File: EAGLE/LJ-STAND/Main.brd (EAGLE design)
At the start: 100 x 80 mm, 74 parts

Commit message: Things
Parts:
- removed MTR2_OUT1, MTR3_OUT2: (no value), jst-vh:B2P-VH
- added MTR2_OUT, MTR3_OUT: (no value), jst-vh:B2P-VH
- added PIXY_I2C, PIXY_SPI: (no value), SparkFun-Connectors:2X5-SHROUDED
- added R3, R4: 4.7K, SparkFun-Resistors:0603-RES
- moved IMU 133.5 mm to (-38.1, 115.6)
- moved R2 132.9 mm to (-54.6, 115.6)
- moved R1 131.8 mm to (-50.8, 115.6)
- moved MOTOR_3 102.9 mm to (-99.1, 14.0)
- moved C28 86.4 mm to (-101.6, 91.4)
- moved TSOP8 79.6 mm to (-96.5, 102.9)
- moved TSOP16 71.7 mm to (-88.9, 111.8)
- moved C17 61.1 mm to (-19.1, 121.9)
- moved C16 61.1 mm to (-15.2, 121.9)
- moved C21 61.1 mm to (-34.3, 121.9)
- moved C22 61.1 mm to (-38.1, 121.9)
- moved C18 61.1 mm to (-22.9, 121.9)
- moved C19 61.1 mm to (-26.7, 121.9)
- moved C20 61.1 mm to (-30.5, 121.9)
- moved C3 31.9 mm to (-66.0, 115.6)
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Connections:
- new net PIXY_CS: MASTER.43, PIXY_SPI.7
- new net PIXY_MISO: MASTER.45, PIXY_SPI.1
- new net PIXY_MOSI: MASTER.44, PIXY_SPI.4
- new net PIXY_SCK: MASTER.46, PIXY_SPI.3
- new net PIXY_SCL: PIXY_I2C.5
- new net PIXY_SDA: PIXY_I2C.9
- new net TEENSY_SCL: MASTER.37, R3.1
- new net TEENSY_SDA: MASTER.38, R4.1
- net +3V3: now also R3.2, R4.2
- net +5V: now also PIXY_I2C.2, PIXY_SPI.2
- net CS_LIGHT_SENSOR: now also LIGHT_SENSOR.10
- net CS_TSOP: now also MASTER.21; no longer MASTER.15
- net GND: now also PIXY_I2C.10, PIXY_I2C.6, PIXY_I2C.8, PIXY_SPI.10, PIXY_SPI.6, PIXY_SPI.8
- net MISO: now also LIGHT_SENSOR.12
- net MOSI: now also LIGHT_SENSOR.11
- net N$1: now also MTR2_OUT.2; no longer MTR2_OUT1.2
- net N$14: now also MTR3_OUT.2; no longer MTR3_OUT2.2
- net N$16: now also MTR3_OUT.1; no longer MTR3_OUT2.1
- net N$2: now also MTR2_OUT.1; no longer MTR2_OUT1.1
- net SCK: now also LIGHT_SENSOR.13
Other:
- board size 100 x 80 mm -> 127.3 x 135.9 mm

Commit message: Stuffs
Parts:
- added Q1, Q2: BSS138, m-pad-2.1:SOT23
- VREG-3.3V: value LM340S-05 -> LM1084
- moved LOGIC_FUSE 121.5 mm to (-123.2, -17.8)
- moved MOTOR_FUSE 105.7 mm to (-123.2, -7.62)
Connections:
- new net TEENSY_SDL: TSOP.37
- net TEENSY_SCL: now also LIGHT_SENSOR.3
- net TEENSY_SDA: now also LIGHT_SENSOR.4, TSOP.38
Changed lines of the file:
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@@
 <?xml version="1.0" encoding="utf-8"?>
 <!DOCTYPE eagle SYSTEM "eagle.dtd">
-<eagle version="7.5.0">
+<eagle version="7.2.0">
 <drawing>
 <settings>
@@
 </element>
 <element name="LIGHT_SENSOR" library="teensy-3.5" package="TEENSY-3.5" value="TEENSY-3.5" x="-22.86" y="31.75"/>
-<element name="LOGIC_FUSE" library="fuse-holder-3568" package="3568-FUSEHOLDER" value="2A" x="-69.85" y="91.44"/>
 <element name="LOGIC_SWITCH" library="jst-vh" package="B2P-VH" value="" x="-74.93" y="69.85"/>
 <element name="MASTER" library="teensy-3.5" package="TEENSY-3.5" value="TEENSY-3.5" x="-41.91" y="31.75"/>
@@
 <element name="MOTOR_2" library="TB6549PG-motor-controller" package="TB6549PG" value="TB6549PG" x="-87.63" y="13.97"/>
 <element name="MOTOR_3" library="TB6549PG-motor-controller" package="TB6549PG" value="TB6549PG" x="-99.06" y="13.97"/>
-<element name="MOTOR_FUSE" library="fuse-holder-3568" package="3568-FUSEHOLDER" value="7.5A" x="-86.36" y="91.44"/>
 <element name="MOTOR_SWITCH" library="jst-vh" package="B2P-VH" value="" x="-59.69" y="69.85"/>
 <element name="MTR1_OUT" library="jst-vh" package="B2P-VH" value="" x="-20.32" y="92.71"/>
@@
 <element name="TSOP8" library="tsop" package="TSOP17XX" value="TSOP1737" x="-96.52" y="102.87"/>
 <element name="TSOP9" library="tsop" package="TSOP17XX" value="TSOP1737" x="-17.78" y="111.76"/>
-<element name="VREG-3.3V" library="linear" package="TO263-3" value="LM340S-05" x="-40.64" y="72.39"/>
+<element name="VREG-3.3V" library="linear" package="TO263-3" value="LM1084" x="-40.64" y="72.39"/>
 <element name="VREG-5V" library="V78-2000-switching-regulator" package="V78-2000" value="V78-2000" x="-50.8" y="95.25"/>
+<element name="MOTOR_FUSE" library="fuse-holder-3568" package="3568-FUSEHOLDER" value="7.5A" x="-123.19" y="-7.62"/>
+<element name="LOGIC_FUSE" library="fuse-holder-3568" package="3568-FUSEHOLDER" value="2A" x="-123.19" y="-17.78"/>
+<element name="Q1" library="m-pad-2.1" package="SOT23" value="BSS138" x="-124.46" y="-26.67"/>
+<element name="Q2" library="m-pad-2.1" package="SOT23" value="BSS138" x="-124.46" y="-34.29"/>
 </elements>
 <signals>
 <signal name="PWR">
 <contactref element="C1" pad="+"/>
+<contactref element="PWR_IN" pad="2"/>
 <contactref element="MOTOR_FUSE" pad="1"/>
 <contactref element="MOTOR_FUSE" pad="2"/>
 <contactref element="LOGIC_FUSE" pad="1"/>
 <contactref element="LOGIC_FUSE" pad="2"/>
-<contactref element="PWR_IN" pad="2"/>
-<wire x1="-36.83" y1="92.71" x2="-27.23" y2="92.71" width="0" layer="19" extent="1-1"/>
-<wire x1="-69.85" y1="91.44" x2="-36.83" y2="92.71" width="0" layer="19" extent="1-1"/>
-<wire x1="-69.85" y1="94.8436" x2="-69.85" y2="91.44" width="0" layer="19" extent="1-1"/>
-<wire x1="-86.36" y1="94.8436" x2="-69.85" y2="94.8436" width="0" layer="19" extent="1-1"/>
-<wire x1="-86.36" y1="91.44" x2="-86.36" y2="94.8436" width="0" layer="19" extent="1-1"/>
+<wire x1="-123.19" y1="-14.3764" x2="-123.19" y2="-17.78" width="0" layer="19" extent="1-1"/>
+<wire x1="-123.19" y1="-7.62" x2="-123.19" y2="-14.3764" width="0" layer="19" extent="1-1"/>
+<wire x1="-123.19" y1="-4.2164" x2="-123.19" y2="-7.62" width="0" layer="19" extent="1-1"/>
+<wire x1="-36.83" y1="92.71" x2="-123.19" y2="-4.2164" width="0" layer="19" extent="1-1"/>
+<wire x1="-27.23" y1="92.71" x2="-36.83" y2="92.71" width="0" layer="19" extent="1-1"/>
 </signal>
 <signal name="GND">
@@
 </signal>
 <signal name="N$9">
+<contactref element="LOGIC_SWITCH" pad="2"/>
 <contactref element="LOGIC_FUSE" pad="4"/>
 <contactref element="LOGIC_FUSE" pad="3"/>
-<contactref element="LOGIC_SWITCH" pad="2"/>
-<wire x1="-59.944" y1="91.44" x2="-59.944" y2="94.8436" width="0" layer="19" extent="1-1"/>
-<wire x1="-72.95" y1="69.85" x2="-59.944" y2="91.44" width="0" layer="19" extent="1-1"/>
+<wire x1="-113.284" y1="-14.3764" x2="-113.284" y2="-17.78" width="0" layer="19" extent="1-1"/>
+<wire x1="-72.95" y1="69.85" x2="-113.284" y2="-14.3764" width="0" layer="19" extent="1-1"/>
 </signal>
 <signal name="TSOP1">
@@
 </signal>
 <signal name="N$21">
+<contactref element="MOTOR_SWITCH" pad="1"/>
 <contactref element="MOTOR_FUSE" pad="4"/>
-<contactref element="MOTOR_SWITCH" pad="1"/>
 <contactref element="MOTOR_FUSE" pad="3"/>
-<wire x1="-76.454" y1="91.44" x2="-76.454" y2="94.8436" width="0" layer="19" extent="1-1"/>
-<wire x1="-61.67" y1="69.85" x2="-76.454" y2="91.44" width="0" layer="19" extent="1-1"/>
+<wire x1="-113.284" y1="-4.2164" x2="-113.284" y2="-7.62" width="0" layer="19" extent="1-1"/>
+<wire x1="-61.67" y1="69.85" x2="-113.284" y2="-4.2164" width="0" layer="19" extent="1-1"/>
 </signal>
 <signal name="LS1">
@@
 <contactref element="MASTER" pad="38"/>
 <contactref element="R4" pad="1"/>
-<wire x1="-34.29" y1="15.24" x2="-63.08" y2="115.57" width="0" layer="19" extent="1-1"/>
+<contactref element="TSOP" pad="38"/>
+<contactref element="LIGHT_SENSOR" pad="4"/>
+<wire x1="-30.48" y1="48.26" x2="-63.08" y2="115.57" width="0" layer="19" extent="1-1"/>
+<wire x1="-34.29" y1="15.24" x2="-30.48" y2="48.26" width="0" layer="19" extent="1-1"/>
+<wire x1="-53.34" y1="15.24" x2="-34.29" y2="15.24" width="0" layer="19" extent="1-1"/>
 </signal>
 <signal name="TEENSY_SCL">
 <contactref element="MASTER" pad="37"/>
 <contactref element="R3" pad="1"/>
-<wire x1="-34.29" y1="12.7" x2="-59.27" y2="115.57" width="0" layer="19" extent="1-1"/>
+<contactref element="LIGHT_SENSOR" pad="3"/>
+<wire x1="-30.48" y1="50.8" x2="-59.27" y2="115.57" width="0" layer="19" extent="1-1"/>
+<wire x1="-34.29" y1="12.7" x2="-30.48" y2="50.8" width="0" layer="19" extent="1-1"/>
 </signal>
 <signal name="PIXY_MISO">
@@
 <contactref element="PIXY_I2C" pad="9"/>
 </signal>
+<signal name="TEENSY_SDL">
+<contactref element="TSOP" pad="37"/>
+</signal>
 </signals>

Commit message: Logic level converters
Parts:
- added C40, C41, C42, C43, C44, C45, C46, C47: 0.1uF, SparkFun-Capacitors:0603-CAP
- added R5, R6, R7, R8: 10K, SparkFun-Resistors:0603-RES
- added TSOP17, TSOP18, TSOP19, TSOP20, TSOP21, TSOP22, TSOP23, TSOP24: TSOP1737, tsop:TSOP17XX
- moved Q1 21.6 mm to (-124.5, -48.3)
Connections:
- removed net LS25: LIGHT_SENSOR.50
- removed net PIXY_SCL: PIXY_I2C.5
- removed net PIXY_SDA: PIXY_I2C.9
- new net SENSOR_SCL_5V: PIXY_I2C.5, Q1.3, R8.1
- new net SENSOR_SDA_5V: PIXY_I2C.9, Q2.3, R6.1
- new net TSOP17: TSOP.20, TSOP17.OUT
- new net TSOP18: TSOP.21, TSOP18.OUT
- new net TSOP19: TSOP.22, TSOP19.OUT
- new net TSOP20: TSOP.23, TSOP20.OUT
- new net TSOP21: TSOP.24, TSOP21.OUT
- new net TSOP22: TSOP.25, TSOP22.OUT
- new net TSOP23: TSOP.26, TSOP23.OUT
- new net TSOP24: TSOP.27, TSOP24.OUT
- net +3V3: now also Q1.1, Q2.1, R5.2, R7.2
- net +5V: now also R6.2, R8.2
- net GND: now also C40.2, C41.2, C42.2, C43.2, C44.2, C45.2, C46.2, C47.2, TSOP17.GND, TSOP18.GND, TSOP19.GND, TSOP20.GND, TSOP21.GND, TSOP22.GND, TSOP23.GND, TSOP24.GND
- net SENSOR_SCL: now also Q1.2, R7.1
- net SENSOR_SDA: now also Q2.2, R5.1
- net TSOP_PWR: now also C40.1, C41.1, C42.1, C43.1, C44.1, C45.1, C46.1, C47.1, TSOP.28, TSOP.29, TSOP.30, TSOP.31, TSOP17.V+, TSOP18.V+, TSOP19.V+, TSOP20.V+, TSOP21.V+, TSOP22.V+, TSOP23.V+, TSOP24.V+; no longer TSOP.20, TSOP.21, TSOP.22, TSOP.23

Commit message: PCB
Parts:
- removed LIGHT_SENSOR: TEENSY-3.5, teensy-3.5:TEENSY-3.5
- added BLUETOOTH: (no value), SparkFun-Connectors:1X06
- added LED1: BLUE, adafruit:CHIPLED_0603
- added LED2, LED3, LED4, LED5: GREEN, adafruit:CHIPLED_0603
- added LIGHT_SENSOR_CONNECTOR: (no value), pinhead+:2X13_SMT
- added R10, R11, R12, R13, R14, R15, R16, R9: 10K, SparkFun-Resistors:0603-RES
- added R17, R18, R19, R20, R21: 330, SparkFun-Resistors:0603-RES
- added SLAVE_LIGHT: TEENSY-3.5, teensy-3.5:TEENSY-3.5
- added SW1: (no value), SparkFun-Electromechanical:DIPSWITCH-08
- added XBEE: XBEE, adafruit:XBEE
- LOGIC_SWITCH, MOTOR_SWITCH, MTR1_OUT, MTR2_OUT, MTR3_OUT, PWR_IN: value (none) -> VH
- moved C47 249.5 mm to (-22.9, 141.0)
- moved C45 243.0 mm to (-15.2, 141.0)
- moved C46 240.1 mm to (-19.1, 141.0)
- moved TSOP21 224.9 mm to (-17.8, 129.5)
- moved TSOP23 222.2 mm to (-38.1, 129.5)
- moved C41 220.5 mm to (-106.7, 137.2)
- moved C42 220.0 mm to (-110.5, 137.2)
- moved C43 219.7 mm to (-114.3, 137.2)
- moved C44 219.7 mm to (-118.1, 137.2)
- moved TSOP22 216.3 mm to (-27.9, 129.5)
- moved TSOP24 215.3 mm to (-48.3, 129.5)
- moved C40 213.4 mm to (-102.9, 137.2)
- moved R7 210.8 mm to (-26.7, 133.3)
- moved R8 207.3 mm to (-30.5, 133.3)
- moved R6 202.6 mm to (-22.9, 133.3)
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- renumbered TSOP to SLAVE_TSOP
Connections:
- new net BT_RX: BLUETOOTH.5, MASTER.33
- new net BT_TX: BLUETOOTH.4, MASTER.34
- new net DIP1: MASTER.24, R9.1, SW1.8
- new net DIP2: MASTER.25, R10.1, SW1.7
- new net DIP3: MASTER.26, R11.1
- new net DIP4: MASTER.27, R12.1, SW1.5
- new net DIP5: MASTER.28, R13.1, SW1.4
- new net DIP6: MASTER.29, R14.1, SW1.3
- new net DIP7: MASTER.30, R15.1, SW1.2
- new net DIP8: MASTER.31, R16.1, SW1.1
- new net LED_1: MASTER.50, R18.2, R20.2
- new net LED_2: MASTER.51, R19.2, R21.2
- new net LED_3: MASTER.52
- new net LED_4: MASTER.53
- new net N$22: SW1.6
- new net N$23: LED3.A, R19.1
- new net N$24: LED4.A, R20.1
- new net N$25: LED5.A, R21.1
- new net N$27: LED1.A, R17.1
- new net N$29: LED2.A, R18.1
- new net XBEE_RX: MASTER.48, XBEE.3
- new net XBEE_TX: MASTER.47, XBEE.2
- net +3V3: now also LIGHT_SENSOR_CONNECTOR.25, R10.2, R11.2, R12.2, R13.2, R14.2, R15.2, R16.2, R9.2, SLAVE_LIGHT.3.3V, XBEE.1; no longer LIGHT_SENSOR.3.3V
- net +5V: now also R17.2
- net CS_LIGHT_SENSOR: now also SLAVE_LIGHT.10; no longer LIGHT_SENSOR.10
- net GND: now also LED1.C, LED2.C, LED3.C, LED4.C, LED5.C, LIGHT_SENSOR_CONNECTOR.26, SLAVE_LIGHT.AGND, SLAVE_LIGHT.GND, SLAVE_LIGHT.GND-1, SLAVE_LIGHT.GND-2, SLAVE_LIGHT.GND-3, SLAVE_LIGHT.GND-4, SW1.10, SW1.11, SW1.12, SW1.13, SW1.14, SW1.15, SW1.16, SW1.9, XBEE.10; no longer LIGHT_SENSOR.AGND, LIGHT_SENSOR.GND, LIGHT_SENSOR.GND-1, LIGHT_SENSOR.GND-2, LIGHT_SENSOR.GND-3, LIGHT_SENSOR.GND-4
- net LS1: now also LIGHT_SENSOR_CONNECTOR.1, SLAVE_LIGHT.14; no longer LIGHT_SENSOR.14
- net LS10: now also LIGHT_SENSOR_CONNECTOR.10, SLAVE_LIGHT.23; no longer LIGHT_SENSOR.23
- net LS11: now also LIGHT_SENSOR_CONNECTOR.11, SLAVE_LIGHT.A10; no longer LIGHT_SENSOR.A10
- net LS12: now also LIGHT_SENSOR_CONNECTOR.12, SLAVE_LIGHT.A11; no longer LIGHT_SENSOR.A11
- net LS13: now also LIGHT_SENSOR_CONNECTOR.13, SLAVE_LIGHT.31; no longer LIGHT_SENSOR.31
- net LS14: now also LIGHT_SENSOR_CONNECTOR.14, SLAVE_LIGHT.32; no longer LIGHT_SENSOR.32
- net LS15: now also LIGHT_SENSOR_CONNECTOR.15, SLAVE_LIGHT.33; no longer LIGHT_SENSOR.33
- net LS16: now also LIGHT_SENSOR_CONNECTOR.16, SLAVE_LIGHT.34; no longer LIGHT_SENSOR.34
- net LS17: now also LIGHT_SENSOR_CONNECTOR.17, SLAVE_LIGHT.35; no longer LIGHT_SENSOR.35
- net LS18: now also LIGHT_SENSOR_CONNECTOR.18, SLAVE_LIGHT.36; no longer LIGHT_SENSOR.36
- net LS19: now also LIGHT_SENSOR_CONNECTOR.19, SLAVE_LIGHT.37; no longer LIGHT_SENSOR.37
- net LS2: now also LIGHT_SENSOR_CONNECTOR.2, SLAVE_LIGHT.15; no longer LIGHT_SENSOR.15
- net LS20: now also LIGHT_SENSOR_CONNECTOR.20, SLAVE_LIGHT.38; no longer LIGHT_SENSOR.38
- net LS21: now also LIGHT_SENSOR_CONNECTOR.21, SLAVE_LIGHT.39; no longer LIGHT_SENSOR.39
- net LS22: now also LIGHT_SENSOR_CONNECTOR.22, SLAVE_LIGHT.DA0; no longer LIGHT_SENSOR.DA0
- net LS23: now also LIGHT_SENSOR_CONNECTOR.23, SLAVE_LIGHT.DA1; no longer LIGHT_SENSOR.DA1
- net LS24: now also LIGHT_SENSOR_CONNECTOR.24, SLAVE_LIGHT.49; no longer LIGHT_SENSOR.49
- net LS3: now also LIGHT_SENSOR_CONNECTOR.3, SLAVE_LIGHT.16; no longer LIGHT_SENSOR.16
- net LS4: now also LIGHT_SENSOR_CONNECTOR.4, SLAVE_LIGHT.17; no longer LIGHT_SENSOR.17
- net LS5: now also LIGHT_SENSOR_CONNECTOR.5, SLAVE_LIGHT.18; no longer LIGHT_SENSOR.18
- net LS6: now also LIGHT_SENSOR_CONNECTOR.6, SLAVE_LIGHT.19; no longer LIGHT_SENSOR.19
- net LS7: now also LIGHT_SENSOR_CONNECTOR.7, SLAVE_LIGHT.20; no longer LIGHT_SENSOR.20
- net LS8: now also LIGHT_SENSOR_CONNECTOR.8, SLAVE_LIGHT.21; no longer LIGHT_SENSOR.21
- net LS9: now also LIGHT_SENSOR_CONNECTOR.9, SLAVE_LIGHT.22; no longer LIGHT_SENSOR.22
- net MISO: now also SLAVE_LIGHT.12; no longer LIGHT_SENSOR.12
- net MOSI: now also SLAVE_LIGHT.11; no longer LIGHT_SENSOR.11
- net SCK: now also SLAVE_LIGHT.13; no longer LIGHT_SENSOR.13
- net TEENSY_SCL: now also SLAVE_LIGHT.3; no longer LIGHT_SENSOR.3
- net TEENSY_SDA: now also SLAVE_LIGHT.4; no longer LIGHT_SENSOR.4
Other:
- board size 127.3 x 135.9 mm -> 160 x 100 mm

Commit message: Eagle stuffs
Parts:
- renumbered TSOP1 to 0, TSOP10 to 17, TSOP11 to 18, TSOP12 to 19, TSOP13 to 20, TSOP14 to 21, TSOP15 to 22, TSOP16 to 23, TSOP17 to 8, TSOP18 to 9, TSOP19 to 10, TSOP2 to 1, TSOP20 to 11, TSOP21 to 12, TSOP22 to 13, TSOP23 to 14, TSOP24 to 15, TSOP3 to 2, TSOP4 to 3, TSOP5 to 4, TSOP6 to 5, TSOP7 to 6, TSOP8 to 7, TSOP9 to 16
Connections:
- removed net LS24: LIGHT_SENSOR_CONNECTOR.24, SLAVE_LIGHT.49
- removed net TSOP24: 15.OUT, SLAVE_TSOP.27
- new net LS0: LIGHT_SENSOR_CONNECTOR.1, SLAVE_LIGHT.14
- new net TSOP0: 0.OUT, SLAVE_TSOP.0
- net LS1: now also LIGHT_SENSOR_CONNECTOR.2, SLAVE_LIGHT.15; no longer LIGHT_SENSOR_CONNECTOR.1, SLAVE_LIGHT.14
- net LS10: now also LIGHT_SENSOR_CONNECTOR.11, SLAVE_LIGHT.A10; no longer LIGHT_SENSOR_CONNECTOR.10, SLAVE_LIGHT.23
- net LS11: now also LIGHT_SENSOR_CONNECTOR.12, SLAVE_LIGHT.A11; no longer LIGHT_SENSOR_CONNECTOR.11, SLAVE_LIGHT.A10
- net LS12: now also LIGHT_SENSOR_CONNECTOR.13, SLAVE_LIGHT.31; no longer LIGHT_SENSOR_CONNECTOR.12, SLAVE_LIGHT.A11
- net LS13: now also LIGHT_SENSOR_CONNECTOR.14, SLAVE_LIGHT.32; no longer LIGHT_SENSOR_CONNECTOR.13, SLAVE_LIGHT.31
- net LS14: now also LIGHT_SENSOR_CONNECTOR.15, SLAVE_LIGHT.33; no longer LIGHT_SENSOR_CONNECTOR.14, SLAVE_LIGHT.32
- net LS15: now also LIGHT_SENSOR_CONNECTOR.16, SLAVE_LIGHT.34; no longer LIGHT_SENSOR_CONNECTOR.15, SLAVE_LIGHT.33
- net LS16: now also LIGHT_SENSOR_CONNECTOR.17, SLAVE_LIGHT.35; no longer LIGHT_SENSOR_CONNECTOR.16, SLAVE_LIGHT.34
- net LS17: now also LIGHT_SENSOR_CONNECTOR.18, SLAVE_LIGHT.36; no longer LIGHT_SENSOR_CONNECTOR.17, SLAVE_LIGHT.35
- net LS18: now also LIGHT_SENSOR_CONNECTOR.19, SLAVE_LIGHT.37; no longer LIGHT_SENSOR_CONNECTOR.18, SLAVE_LIGHT.36
- net LS19: now also LIGHT_SENSOR_CONNECTOR.20, SLAVE_LIGHT.38; no longer LIGHT_SENSOR_CONNECTOR.19, SLAVE_LIGHT.37
- net LS2: now also LIGHT_SENSOR_CONNECTOR.3, SLAVE_LIGHT.16; no longer LIGHT_SENSOR_CONNECTOR.2, SLAVE_LIGHT.15
- net LS20: now also LIGHT_SENSOR_CONNECTOR.21, SLAVE_LIGHT.39; no longer LIGHT_SENSOR_CONNECTOR.20, SLAVE_LIGHT.38
- net LS21: now also LIGHT_SENSOR_CONNECTOR.22, SLAVE_LIGHT.DA0; no longer LIGHT_SENSOR_CONNECTOR.21, SLAVE_LIGHT.39
- net LS22: now also LIGHT_SENSOR_CONNECTOR.23, SLAVE_LIGHT.DA1; no longer LIGHT_SENSOR_CONNECTOR.22, SLAVE_LIGHT.DA0
- net LS23: now also LIGHT_SENSOR_CONNECTOR.24, SLAVE_LIGHT.49; no longer LIGHT_SENSOR_CONNECTOR.23, SLAVE_LIGHT.DA1
- net LS3: now also LIGHT_SENSOR_CONNECTOR.4, SLAVE_LIGHT.17; no longer LIGHT_SENSOR_CONNECTOR.3, SLAVE_LIGHT.16
- net LS4: now also LIGHT_SENSOR_CONNECTOR.5, SLAVE_LIGHT.18; no longer LIGHT_SENSOR_CONNECTOR.4, SLAVE_LIGHT.17
- net LS5: now also LIGHT_SENSOR_CONNECTOR.6, SLAVE_LIGHT.19; no longer LIGHT_SENSOR_CONNECTOR.5, SLAVE_LIGHT.18
- net LS6: now also LIGHT_SENSOR_CONNECTOR.7, SLAVE_LIGHT.20; no longer LIGHT_SENSOR_CONNECTOR.6, SLAVE_LIGHT.19
- net LS7: now also LIGHT_SENSOR_CONNECTOR.8, SLAVE_LIGHT.21; no longer LIGHT_SENSOR_CONNECTOR.7, SLAVE_LIGHT.20
- net LS8: now also LIGHT_SENSOR_CONNECTOR.9, SLAVE_LIGHT.22; no longer LIGHT_SENSOR_CONNECTOR.8, SLAVE_LIGHT.21
- net LS9: now also LIGHT_SENSOR_CONNECTOR.10, SLAVE_LIGHT.23; no longer LIGHT_SENSOR_CONNECTOR.9, SLAVE_LIGHT.22
- net TSOP1: now also 1.OUT, SLAVE_TSOP.1; no longer 0.OUT, SLAVE_TSOP.0
- net TSOP10: now also 10.OUT, SLAVE_TSOP.10; no longer 17.OUT, SLAVE_TSOP.9
- net TSOP11: now also 11.OUT, SLAVE_TSOP.14; no longer 18.OUT, SLAVE_TSOP.10
- net TSOP12: now also 12.OUT, SLAVE_TSOP.16; no longer 19.OUT, SLAVE_TSOP.14
- net TSOP13: now also 13.OUT, SLAVE_TSOP.17; no longer 20.OUT, SLAVE_TSOP.16
- net TSOP14: now also 14.OUT, SLAVE_TSOP.18; no longer 21.OUT, SLAVE_TSOP.17
- net TSOP15: now also 15.OUT, SLAVE_TSOP.19; no longer 22.OUT, SLAVE_TSOP.18
- net TSOP16: now also 16.OUT, SLAVE_TSOP.20; no longer 23.OUT, SLAVE_TSOP.19
- net TSOP17: now also 17.OUT, SLAVE_TSOP.21; no longer 8.OUT, SLAVE_TSOP.20
- net TSOP18: now also 18.OUT, SLAVE_TSOP.22; no longer 9.OUT, SLAVE_TSOP.21
- net TSOP19: now also 19.OUT, SLAVE_TSOP.23; no longer 10.OUT, SLAVE_TSOP.22
- net TSOP2: now also 2.OUT, SLAVE_TSOP.2; no longer 1.OUT, SLAVE_TSOP.1
- net TSOP20: now also 20.OUT, SLAVE_TSOP.24; no longer 11.OUT, SLAVE_TSOP.23
- net TSOP21: now also 21.OUT, SLAVE_TSOP.25; no longer 12.OUT, SLAVE_TSOP.24
- net TSOP22: now also 22.OUT, SLAVE_TSOP.26; no longer 13.OUT, SLAVE_TSOP.25
- net TSOP23: now also 23.OUT, SLAVE_TSOP.27; no longer 14.OUT, SLAVE_TSOP.26
- net TSOP3: now also 3.OUT, SLAVE_TSOP.3; no longer 2.OUT, SLAVE_TSOP.2
- net TSOP4: now also 4.OUT, SLAVE_TSOP.4; no longer 3.OUT, SLAVE_TSOP.3
- net TSOP5: now also 5.OUT, SLAVE_TSOP.5; no longer 4.OUT, SLAVE_TSOP.4
- net TSOP6: now also 6.OUT, SLAVE_TSOP.6; no longer 5.OUT, SLAVE_TSOP.5
- net TSOP7: now also 7.OUT, SLAVE_TSOP.7; no longer 6.OUT, SLAVE_TSOP.6
- net TSOP8: now also 8.OUT, SLAVE_TSOP.8; no longer 7.OUT, SLAVE_TSOP.7
- net TSOP9: now also 9.OUT, SLAVE_TSOP.9; no longer 16.OUT, SLAVE_TSOP.8

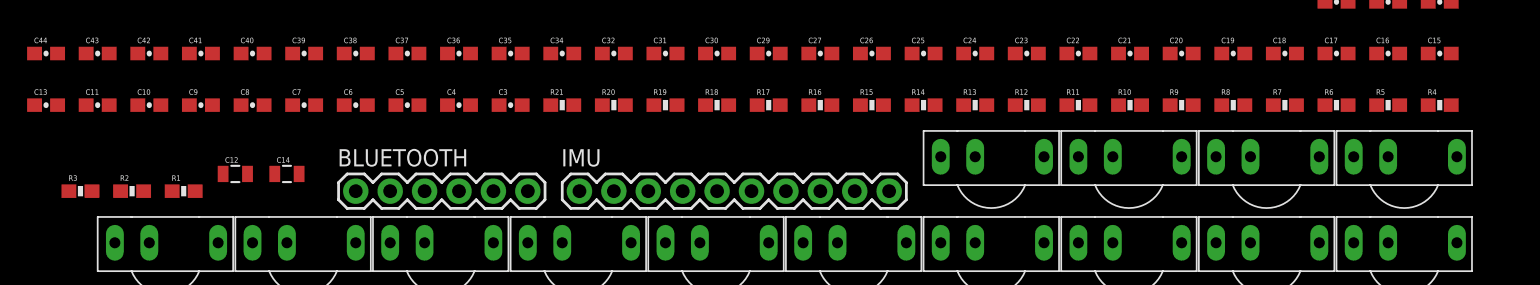
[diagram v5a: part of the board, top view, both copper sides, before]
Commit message: Combined I2C & SPI buses into one of each
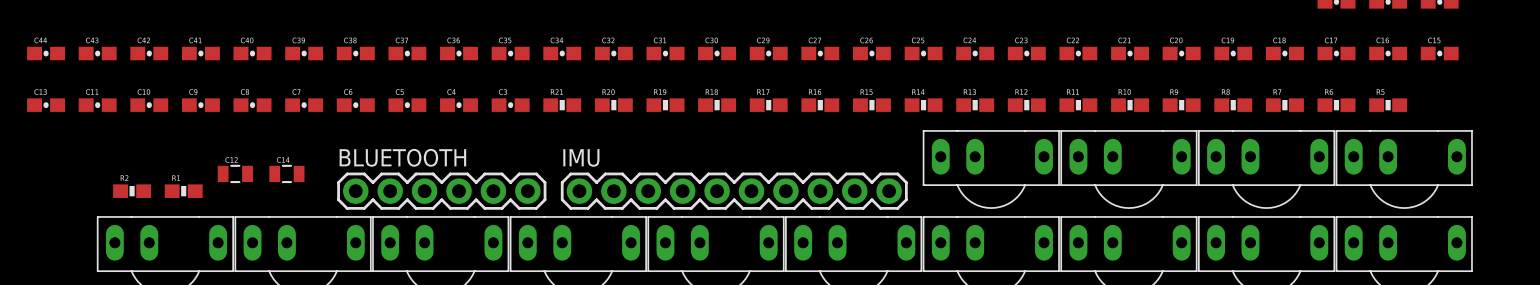
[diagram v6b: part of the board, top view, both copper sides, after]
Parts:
- removed R3, R4: 4.7K, SparkFun-Resistors:0603-RES
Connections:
- net SENSOR_SCL_5V renamed SCL_5V
- net SENSOR_SDA_5V renamed SDA_5V
- removed net PIXY_CS: MASTER.43, PIXY_SPI.7
- removed net PIXY_MISO: MASTER.45, PIXY_SPI.1
- removed net PIXY_MOSI: MASTER.44, PIXY_SPI.4
- removed net PIXY_SCK: MASTER.46, PIXY_SPI.3
- removed net SENSOR_SCL: IMU.3, MASTER.19, Q1.2, R1.1, R7.1
- removed net SENSOR_SDA: IMU.4, MASTER.18, Q2.2, R2.1, R5.1
- removed net TEENSY_SCL: MASTER.37, R3.1, SLAVE_LIGHT.3
- removed net TEENSY_SDA: MASTER.38, R4.1, SLAVE_LIGHT.4, SLAVE_TSOP.38
- removed net TEENSY_SDL: SLAVE_TSOP.37
- new net CS_PIXY: MASTER.15, PIXY_SPI.7
- new net SCL: IMU.3, MASTER.19, Q1.2, R1.1, R7.1, SLAVE_LIGHT.3, SLAVE_TSOP.37
- new net SDA: IMU.4, MASTER.18, MASTER.38, Q2.2, R2.1, R5.1, SLAVE_LIGHT.4, SLAVE_TSOP.38
- net +3V3: no longer R3.2, R4.2
- net MISO: now also PIXY_SPI.1
- net MOSI: now also PIXY_SPI.4
- net SCK: now also PIXY_SPI.3
